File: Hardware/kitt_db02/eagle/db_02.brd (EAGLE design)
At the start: 160 x 100 mm, 30 parts, among them J1 CON_HEADER_1X08-SMD, U1 MCP23017ML

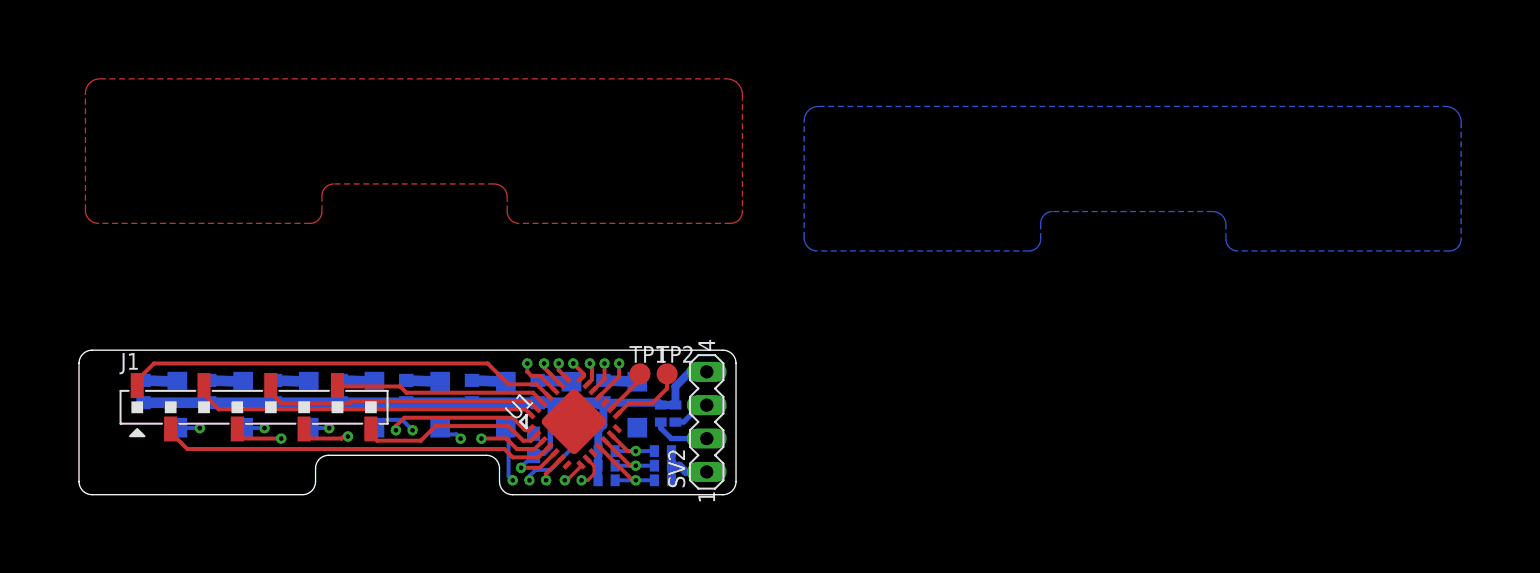
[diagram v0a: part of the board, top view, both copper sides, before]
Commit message: finished bonus board
it's a simple port expander via I2C,
plus it doubles as a neat bar indicator and is as wide as the cart itself.
why indicators? indicates directly the speed and brake-level visually.
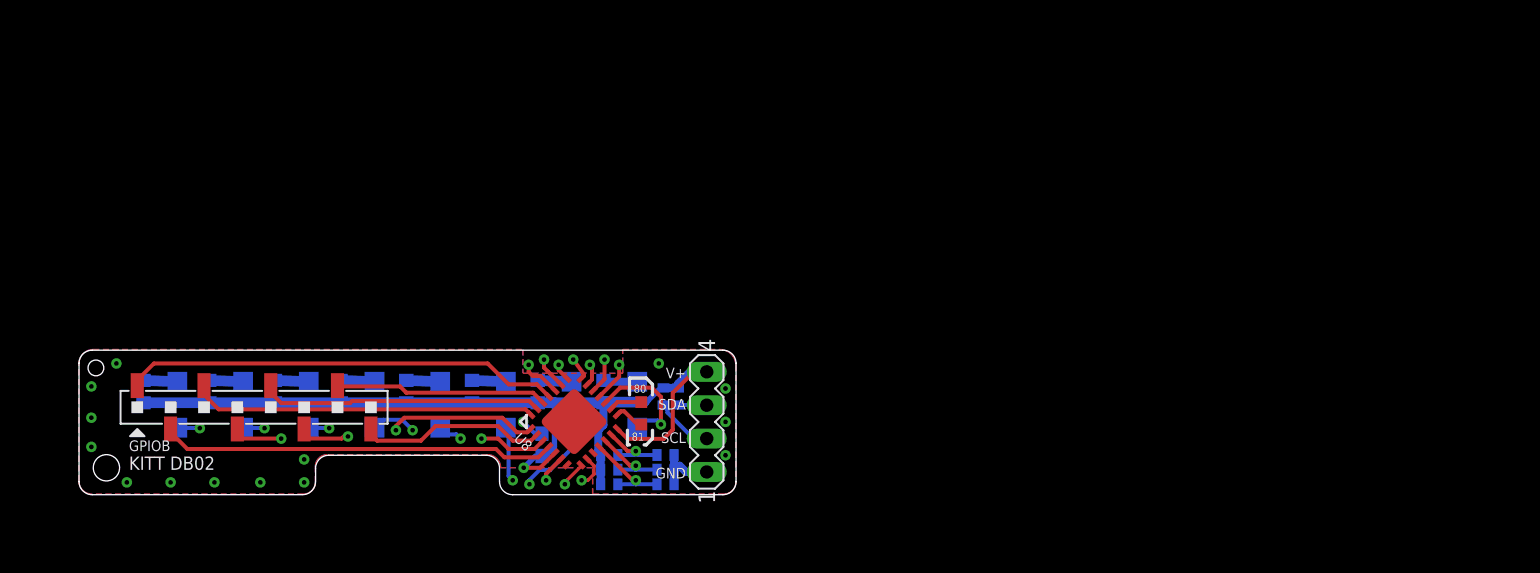
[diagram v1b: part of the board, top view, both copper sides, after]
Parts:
- removed C1.01: 100uF, rcl:C0603
- removed R1.08, R1.09, R1.10, R1.11, R1.12, R1.13, R1.14, R1.15: [10kR], rcl:R0402
- removed TP1, TP2: TPTP16R, testpad:TP16R
- added C8.0: 100uF, rcl:C0603
- added R8.10, R8.11, R8.12, R8.13, R8.14, R8.15, R8.8, R8.9: [10kR], rcl:R0402
- added T8.1, T8.2: TPTP09SQ, testpad:TP09SQ
- renumbered D1.00 to D8.0, D1.01 to D8.1, D1.02 to D8.2, D1.03 to D8.3, D1.04 to D8.4, D1.05 to D8.5, D1.06 to D8.6, D1.07 to D8.7, J1 to X8.1, R1.00 to R8.0, R1.01 to R8.1, R1.02 to R8.2, R1.03 to R8.3, R1.04 to R8.4, R1.05 to R8.5, R1.06 to R8.6, R1.07 to R8.7, SV2 to X8.0, U1 to U8
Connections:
- net GND: now also C8.0.2, R8.11.1, R8.12.1, R8.13.1; no longer C1.01.2, R1.11.1, R1.12.1, R1.13.1
- net N$17: now also R8.11.2, R8.8.1; no longer R1.08.1, R1.11.2
- net N$18: now also R8.12.2, R8.9.1; no longer R1.09.1, R1.12.2
- net N$19: now also R8.10.1, R8.13.2; no longer R1.10.1, R1.13.2
- net N$23: now also T8.1.TP; no longer TP1.TP
- net N$24: now also T8.2.TP; no longer TP2.TP
- net SCL: now also R8.15.1; no longer R1.15.1
- net SDA: now also R8.14.1; no longer R1.14.1
- net V+: now also C8.0.1, R8.10.2, R8.14.2, R8.15.2, R8.8.2, R8.9.2; no longer C1.01.1, R1.08.2, R1.09.2, R1.10.2, R1.14.2, R1.15.2
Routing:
- net V+: track 60.5 -> 70.9 mm
- net N$1: track 0.00 -> 9.27 mm, vias 0 -> 1
- net GND: track 7.22 -> 11.3 mm, vias 1 -> 16
- net N$24: track 5.73 -> 2.34 mm
- net N$5: track 19.9 -> 21.2 mm
- net N$23: track 3.55 -> 2.50 mm
- net N$7: track 26.1 -> 27.0 mm
- net SDA: track 17.9 -> 17.1 mm
- added copper zone on layer 1, net GND
- added copper zone on layer 16, net GND
- removed copper zone on layer 1, net GND1
- removed copper zone on layer 16, net GND2
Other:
- board text added: "80"
- board text added: "81"
- board text added: "ADR"
- board text added: "ESD'16"
- board text added: "GND"
- board text added: "GPIOB"
- board text added: "KITT DB02"
- board text added: "PUP"
- board text added: "SCL"
- board text added: "SDA"
- board text added: "UAS UPPER AUSTRIA"
- board text added: "V+"

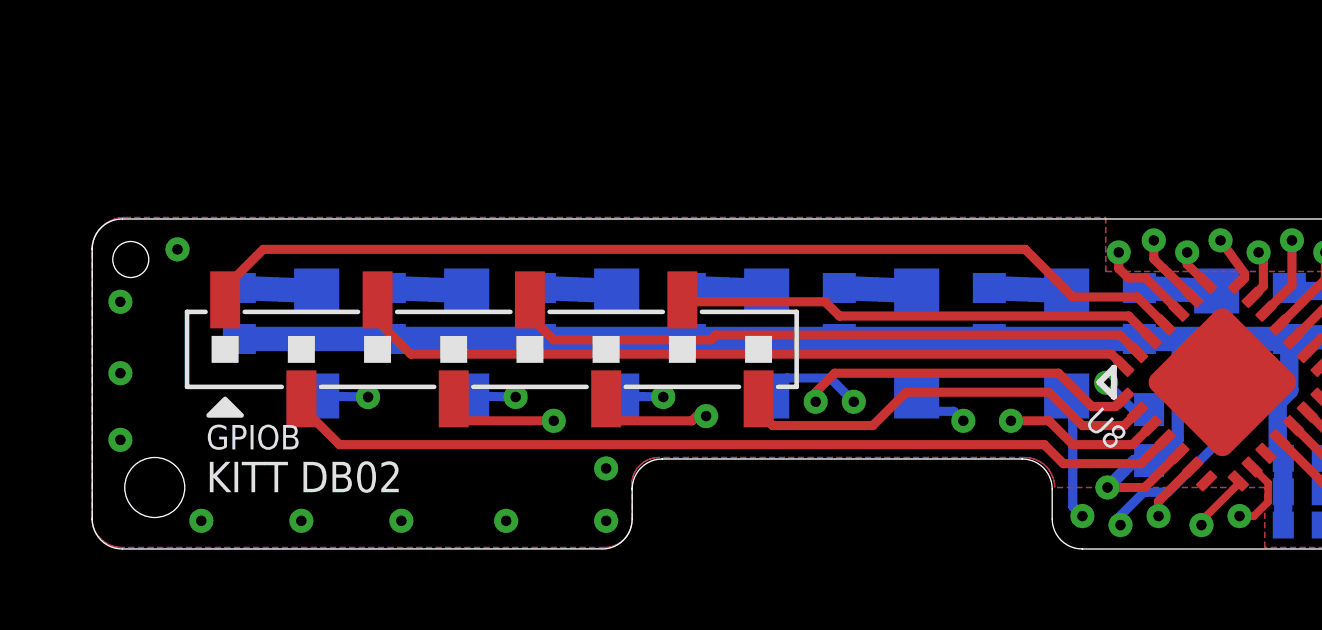
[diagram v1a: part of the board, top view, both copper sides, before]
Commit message: snapshot of db02 board layout -> expanded gpio header to include gnd and supply -> tweaked routing -> added pours, also moved some stiches
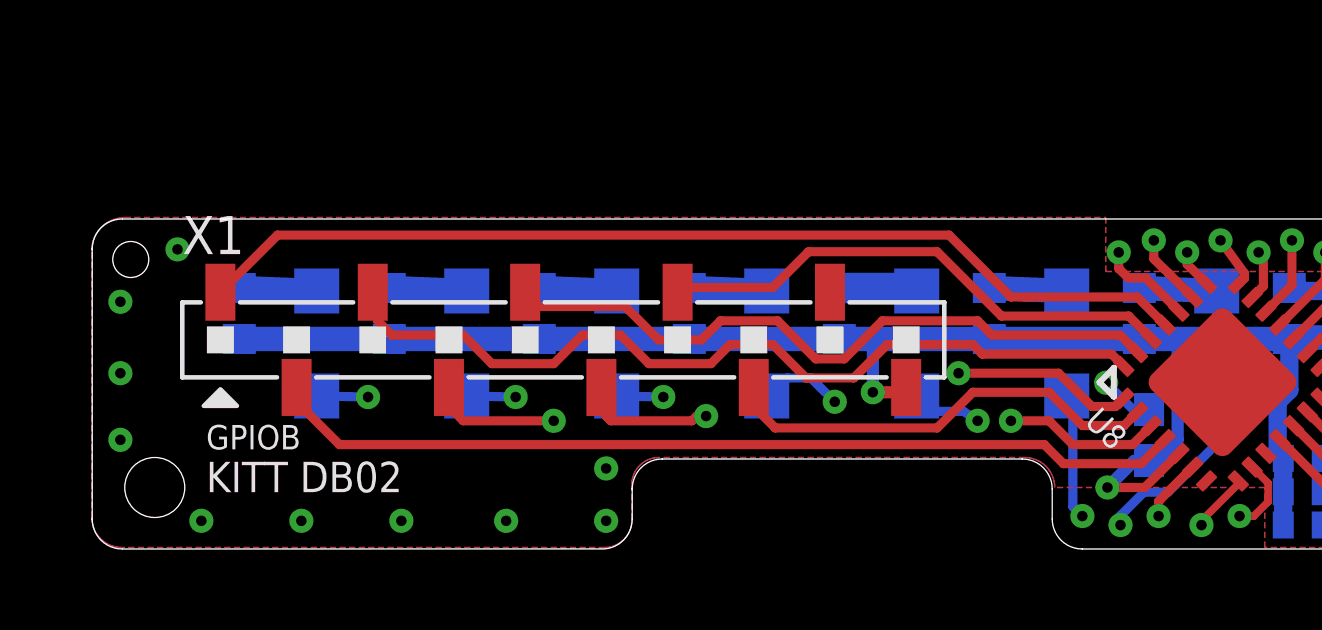
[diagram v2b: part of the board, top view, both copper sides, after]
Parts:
- removed X8.1: CON_HEADER_1X08-SMD, dp_devices:M1X8_SMD
- added X1: CON_HEADER_1X10, kitt.con:M1X10_SMD
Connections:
- net GND: now also X1.P$9
- net GPB0: now also X1.P$1; no longer X8.1.1
- net GPB1: now also X1.P$7; no longer X8.1.7
- net GPB2: now also X1.P$5; no longer X8.1.5
- net GPB3: now also X1.P$3; no longer X8.1.3
- net GPB4: now also X1.P$6; no longer X8.1.6
- net GPB5: now also X1.P$8; no longer X8.1.8
- net GPB6: now also X1.P$4; no longer X8.1.4
- net GPB7: now also X1.P$2; no longer X8.1.2
- net V+: now also X1.P$10
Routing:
- net V+: track 70.9 -> 73.9 mm, vias 1 -> 2
- net GPB3: track 26.2 -> 28.8 mm
- net GPB2: track 21.4 -> 23.3 mm
- net GPB1: track 16.1 -> 17.9 mm
- net N$5: track 21.2 -> 22.5 mm
- net GPB7: track 30.2 -> 30.7 mm

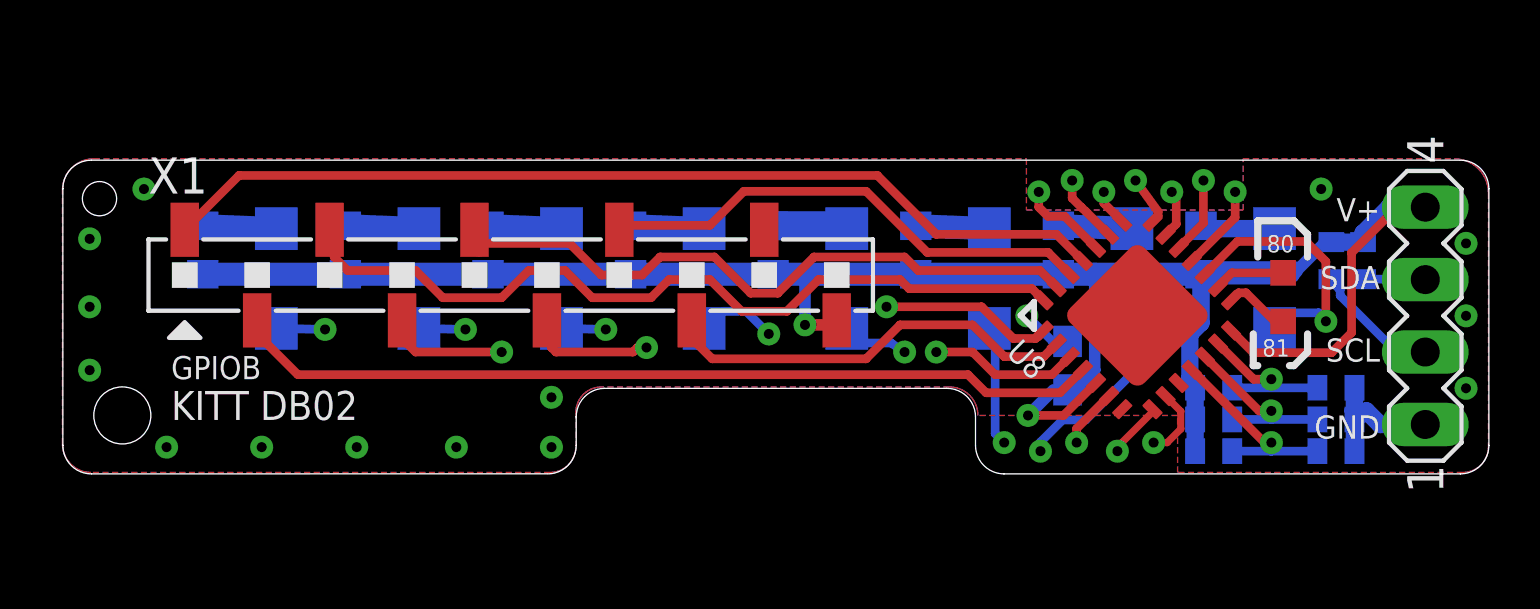
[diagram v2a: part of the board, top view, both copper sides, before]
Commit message: added ©-notice and dash in name to be consistent across boards
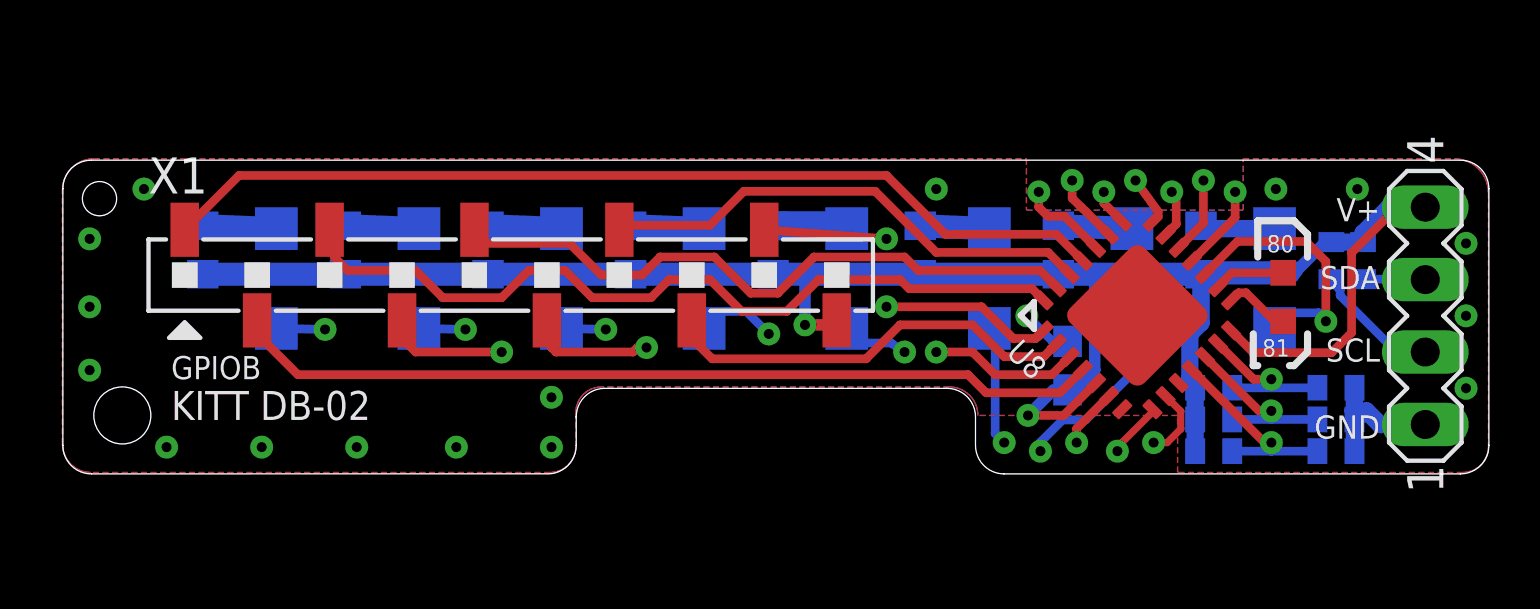
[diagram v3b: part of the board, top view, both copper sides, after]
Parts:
- moved R8.2 0.16 mm to (40.1, 18.5)
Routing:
- net GND: track 11.3 -> 15.6 mm, vias 16 -> 19
- net N$7: track 27.0 -> 28.2 mm
- net N$6: track 22.1 -> 22.7 mm
- net N$8: track 30.6 -> 31.2 mm
- added copper zone on layer 2, net GND
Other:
- board text added: "2017"
- board text added: "C"
- board text added: "KITT DB-02"
- board text removed: "KITT DB02"
